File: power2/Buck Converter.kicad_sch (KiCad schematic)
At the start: 21 parts, among them IC1 TPS56C230RJER, J1 282837-2, J2 76825-0002

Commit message: Feat[power2]: first draft
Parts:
- removed D1: D, Diode_SMD:D_0603_1608Metric, symbol Device:D
- removed J2: 76825-0002, 768250002, symbol 76825-0002:76825-0002
- added C5: C, Capacitor_SMD:C_0402_1005Metric, symbol Device:C
- added J2: 282837-2, 282837-2:TE_282837-2, symbol 282837-2:282837-2
- C2, C3: footprint Capacitor_SMD:C_0805_2012Metric -> Capacitor_SMD:C_1206_3216Metric
- J1: footprint 2828372 -> 282837-2:TE_282837-2; AVAILABILITY (none) -> Good; Arrow Part Number 282837-2 -> (none); Arrow Price/Stock https://www.arrow.com/en/products/282837-2/te-connectivity?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 -> (none); DESCRIPTION (none) -> TERMINAL BLOCK 3.5MM 2POS PCB; Height 10.3 -> (none); MF (none) -> On Shore; MP (none) -> OSTTE020104; Manufacturer_Name TE Connectivity -> (none); Manufacturer_Part_Number 282837-2 -> (none); Mouser Part Number 571-2828372 -> (none); Mouser Price/Stock https://www.mouser.co.uk/ProductDetail/TE-Connectivity/2828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 -> (none); PACKAGE (none) -> None; PARTREV (none) -> G3; PRICE (none) -> 0.28 USD
- R1: value 51.1kΩ -> 51k
- R2: value 102kΩ -> 102k
- R3: renamed from 100kΩ1; value R -> 100k
- R4: value 110kΩ -> 110k
- R5: value 15kΩ -> 15k
- R6: value 15kΩ -> 15kΩ
- R7: renamed from R8; value 330kΩ -> 330k
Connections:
- net GND: now also J1.1, J2.2
- net V_{IN}: no longer C1.2, C2.2, C3.2, IC1.2 (VIN_1), IC1.3 (VIN_2), IC1.4 (VIN_3), IC1.5 (VIN_4), R2.1
- net V_{OUT}: no longer C6.1, C7.1, C8.1, C9.1, L1.2, R4.1
- net at IC1.14 (FB), R4.2, R5.1: now also C5.2
- net at J1.2: now also C1.2, C2.2, C3.2, IC1.2 (VIN_1), IC1.3 (VIN_2), IC1.4 (VIN_3), IC1.5 (VIN_4), R2.1
- new net: C5.1, C6.1, C7.1, C8.1, C9.1, J2.1, L1.2, R4.1
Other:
- moved on the sheet: C6, C7, C8, C9

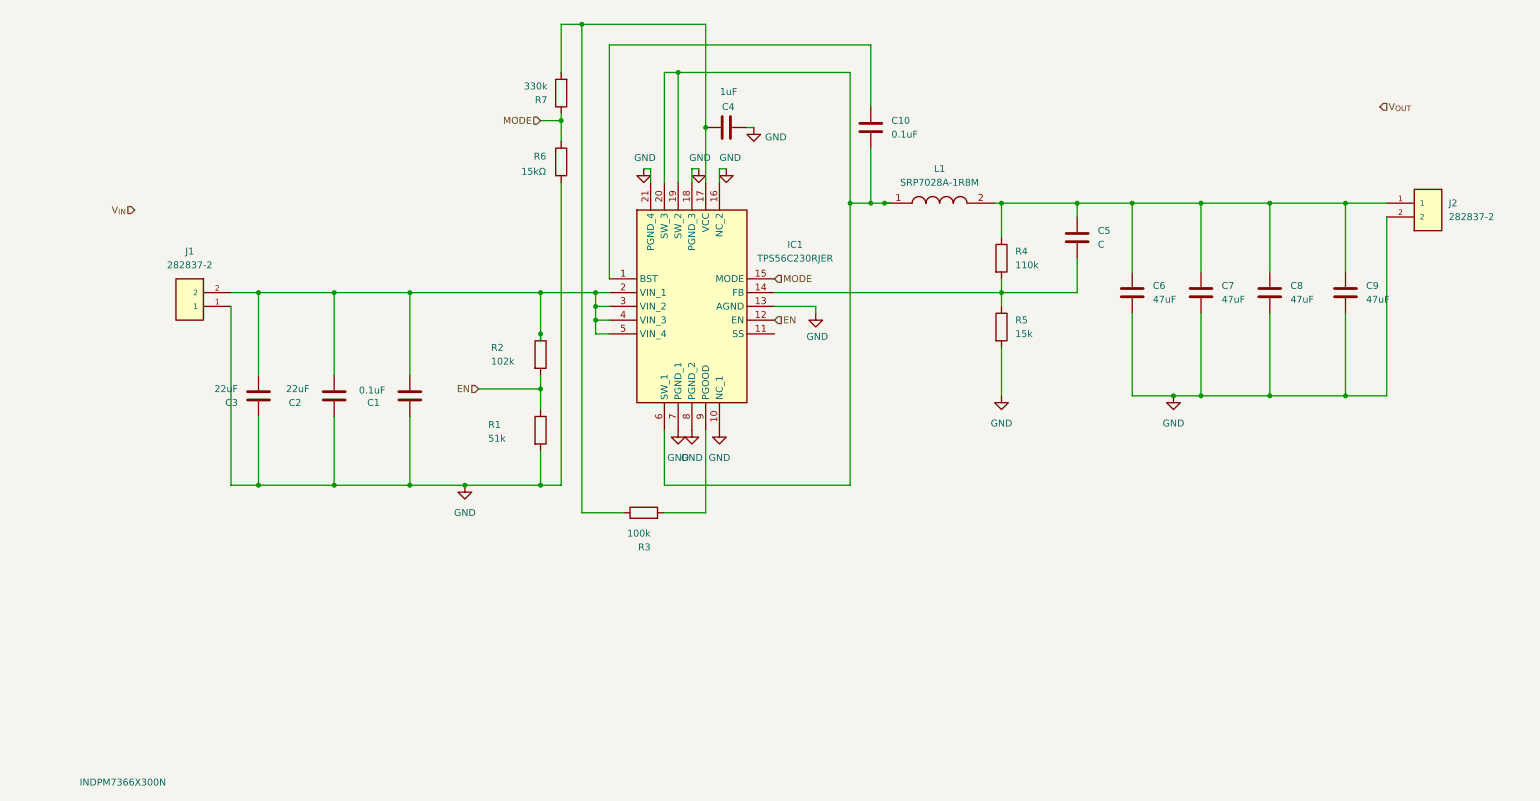
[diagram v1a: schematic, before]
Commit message: Fix: remove bom/cpl from gitignore
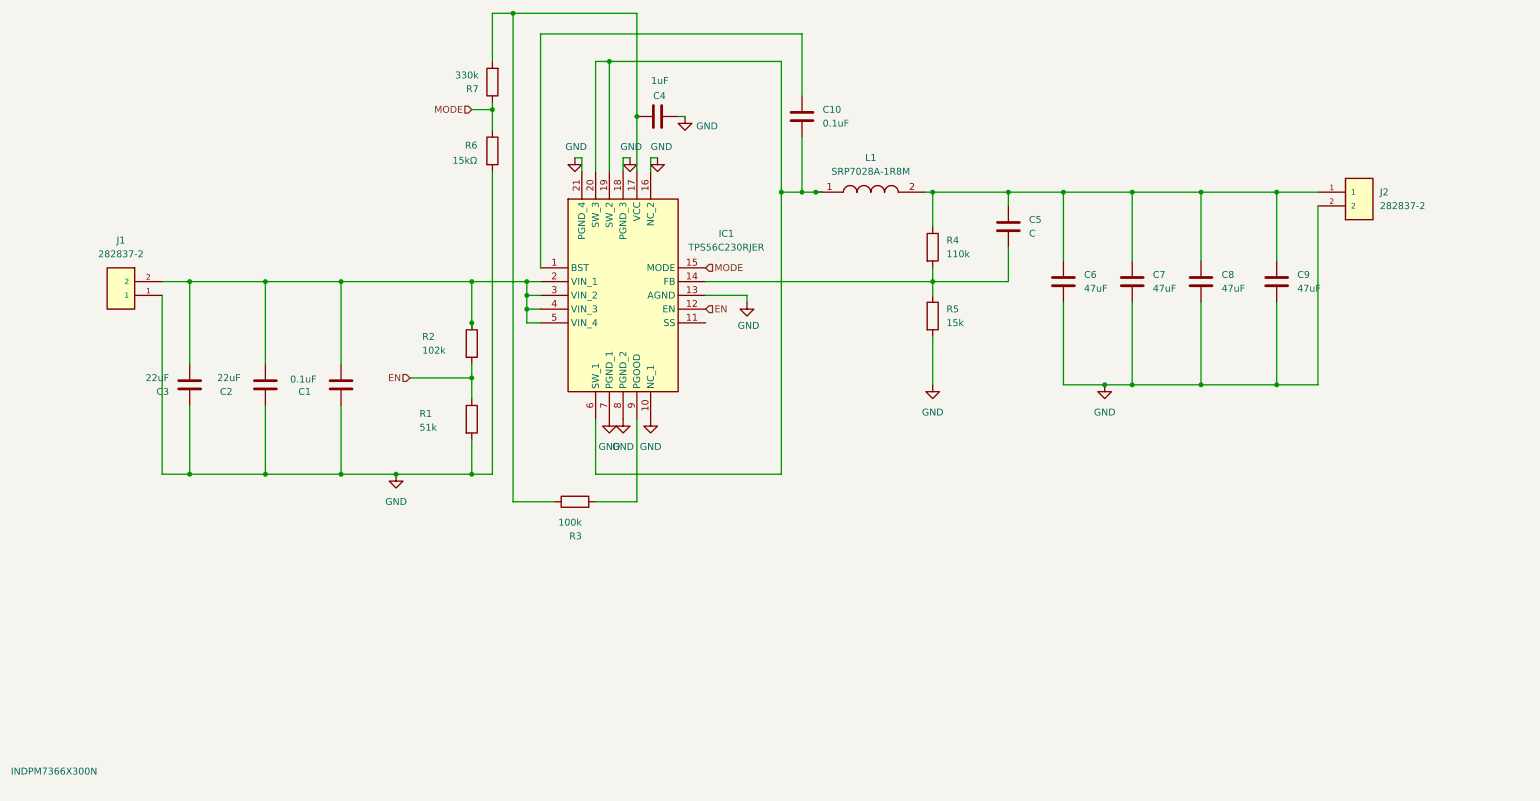
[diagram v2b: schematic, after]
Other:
- company: (none) -> MUREX ROBOTICS [Crane Lee]
- title: (none) -> MUREX 5V Buck Converter
- moved on the sheet: C1, C10, C2, C3, C4, C5, C6, C7, C8, C9, IC1, J1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
